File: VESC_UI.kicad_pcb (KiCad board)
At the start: 4 copper layers, 50 x 50 mm, 60 parts, among them J1 Hall_SS443A, J2 Hall_SS443A, J3 Conn_01x07_Male, J4 Conn_01x09_Female, J5 Conn_01x05_Male, J6 Conn_01x04_Male, J8 Conn_01x02_Male, J9 Conn_01x02_Male, Q1 Q_0010-DVB_Q, Q2 Q_0010-DVB_Q, SW1 SW_Push, SW2 SW_Push, SW3 SW_Push, SW4 SW_Push, SW5 SW_Push, U2 STM32F401CEUx, U3 M95M04-DR, Y1 Crystal_GND24_Small

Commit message: Modify some areas
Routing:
- added copper zone on B.Cu, net GND
- removed copper zone on B.Cu, net (none)

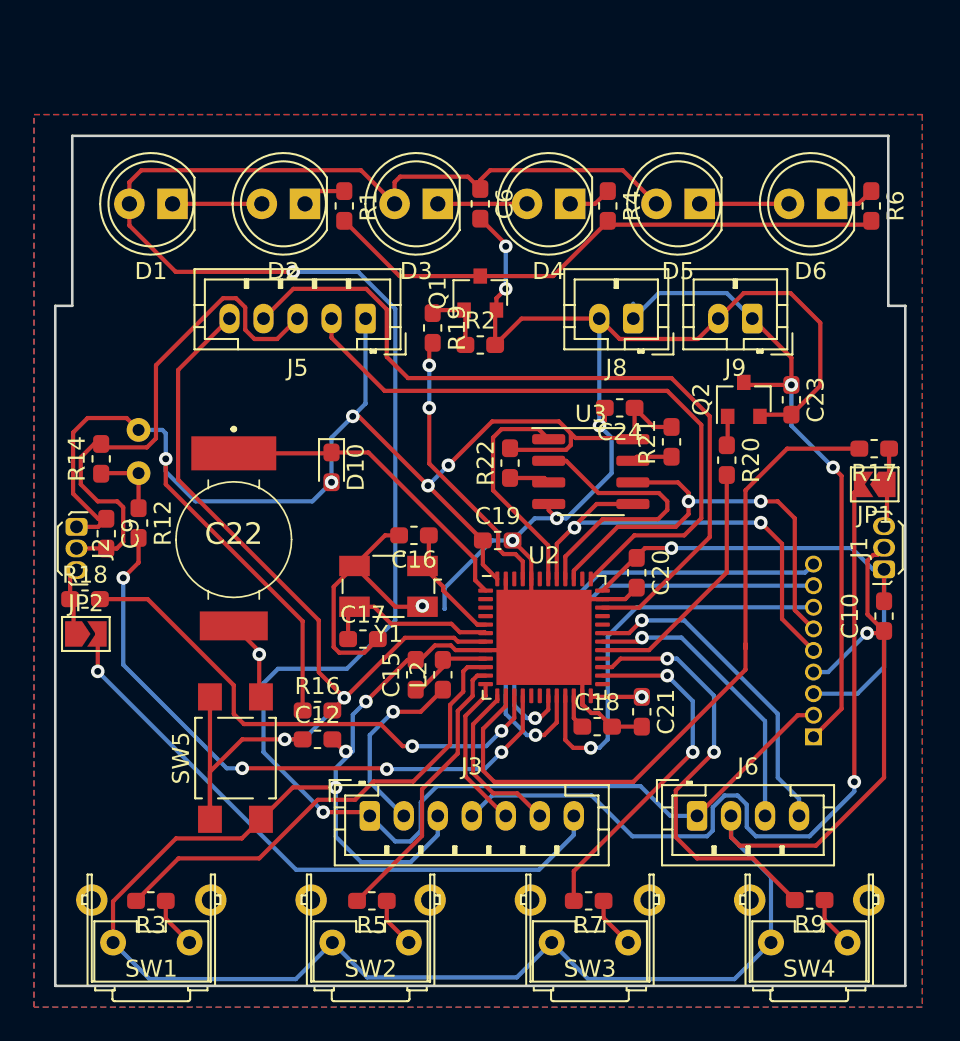
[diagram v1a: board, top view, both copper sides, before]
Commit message: fix: add missing rules and components
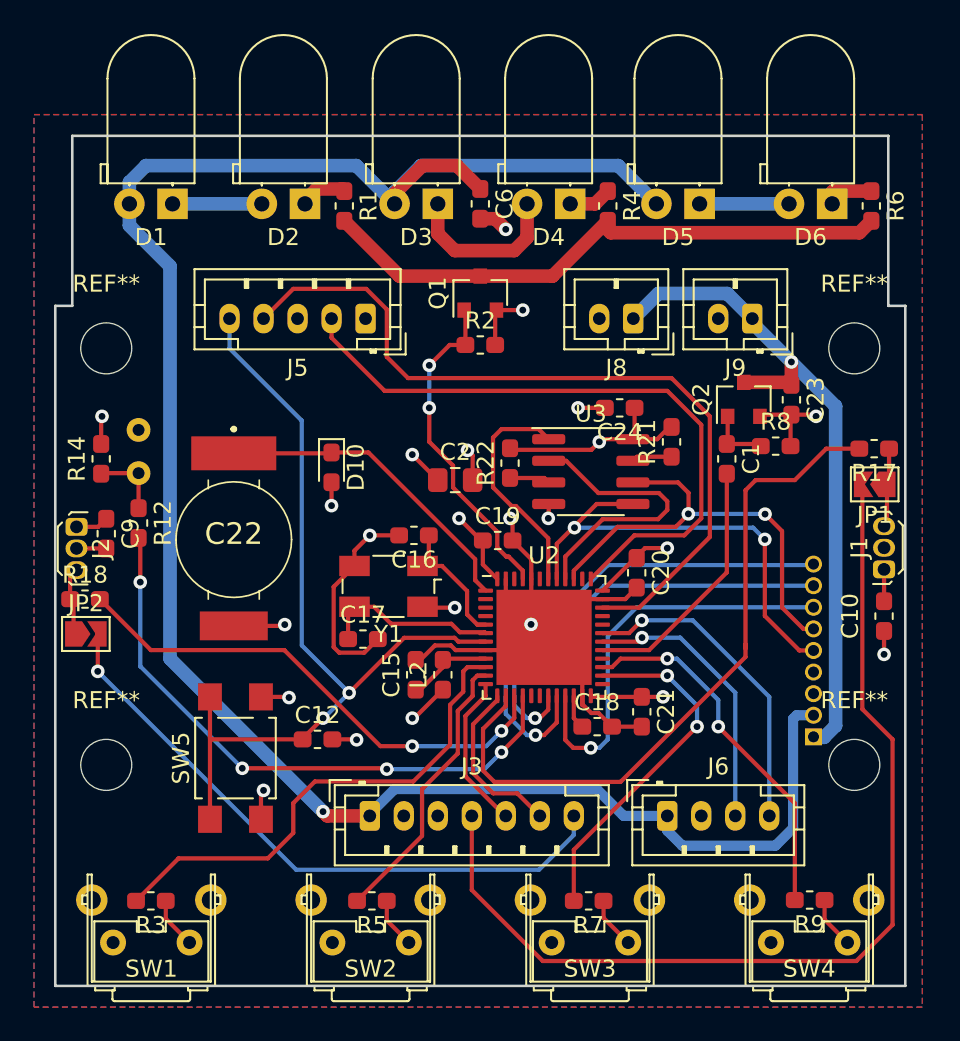
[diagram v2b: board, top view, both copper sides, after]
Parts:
- removed R16: R_Small, Resistor_SMD:R_0603_1608Metric_Pad1.05x0.95mm_HandSolder
- removed R19, R20: R_0020, Resistor_SMD:R_0603_1608Metric_Pad1.05x0.95mm_HandSolder
- added C1: C_Small, Capacitor_SMD:C_0603_1608Metric_Pad1.05x0.95mm_HandSolder, F.Cu at (153.5, 94.0)
- added C2: C_0003-DVB_C, Capacitor_SMD:C_0805_2012Metric_Pad1.15x1.40mm_HandSolder, F.Cu at (137.5, 95.2)
- added R8: R_Small, Resistor_SMD:R_0603_1608Metric_Pad1.05x0.95mm_HandSolder, F.Cu at (156.4, 93.2)
- added REF**: MountingHole_3.2mm_M3_DIN965, MountingHole:MountingHole_3.2mm_M3_DIN965, F.Cu at (161.0, 112.0)
- added REF**: MountingHole_3.2mm_M3_DIN965, MountingHole:MountingHole_3.2mm_M3_DIN965, F.Cu at (117.0, 112.0)
- added REF**: MountingHole_3.2mm_M3_DIN965, MountingHole:MountingHole_3.2mm_M3_DIN965, F.Cu at (117.0, 87.5)
- added REF**: MountingHole_3.2mm_M3_DIN965, MountingHole:MountingHole_3.2mm_M3_DIN965, F.Cu at (161.0, 87.5)
- D1, D2, D3, D4, D5, D6: footprint LED_THT:LED_D5.0mm_Clear -> LED_THT:LED_D5.0mm_Horizontal_O1.27mm_Z3.0mm_Clear
- moved J6 1.75 mm to (150.0, 115.0)
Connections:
- Q1 pad 1: Net-(Q1-Pad1) -> /LIGHT_SW
- R2 pad 1: Net-(Q1-Pad1) -> /LIGHT_SW
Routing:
- net GND: track 277.8 -> 80.4 mm, vias 11 -> 16
- net +3V3: track 137.2 -> 35.8 mm, vias 8 -> 7
- net /Accelerator: track 46.9 -> 58.4 mm, vias 1 -> 0
- net /NRST: track 59.3 -> 51.0 mm
- net +5V: track 127.3 -> 121.8 mm, vias 2 -> 1
- net Net-(D3-Pad1): track 5.25 -> 9.72 mm
- net Net-(Q1-Pad1): track 4.00 -> 0.00 mm
- net /BUTTON_4: track 25.5 -> 21.7 mm
- net /LIGHT_SW: track 16.6 -> 19.6 mm
- net Net-(C1-Pad1): track 1.72 -> 3.70 mm
- net /PHOTO_RESISTOR: track 36.9 -> 35.6 mm
- net /BUTTON_1: track 28.3 -> 29.4 mm
- net /ADC2: track 30.9 -> 30.0 mm
- net /SPI1_SCK: track 27.0 -> 26.2 mm
- net Net-(Q1-Pad3): track 33.9 -> 34.6 mm
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
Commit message: fix: change screen connector footprint and adjust its mechanical position
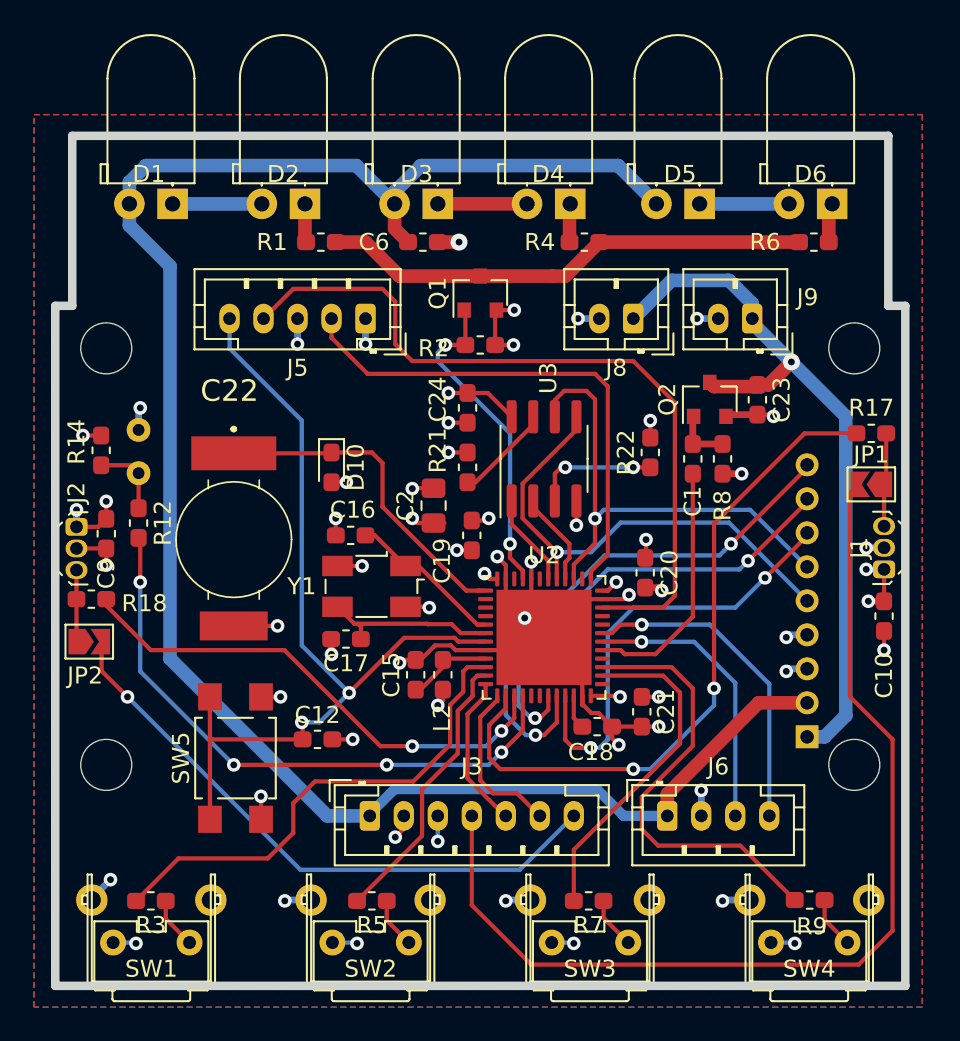
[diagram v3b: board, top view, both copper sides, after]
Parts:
- J4: footprint Connector_PinHeader_1.27mm:PinHeader_1x09_P1.27mm_Vertical -> Connector_PinHeader_2.00mm:PinHeader_1x09_P2.00mm_Vertical
- moved R21 12.1 mm to (138.2, 94.5)
- moved C24 8.95 mm to (138.2, 91.0), turned to 270 degrees
- moved R22 8.27 mm to (149.0, 93.6)
- moved C6 4.06 mm to (135.6, 81.2), turned to 0 degrees
- moved R6 3.99 mm to (158.6, 81.2), turned to 180 degrees
- moved C16 3.72 mm to (131.4, 98.5)
- moved R8 3.21 mm to (153.2, 94.0), turned to 270 degrees
- moved U3 2.85 mm to (142.8, 94.0), turned to 90 degrees
- moved R1 2.53 mm to (129.6, 81.2), turned to 0 degrees
- moved R4 2.53 mm to (145.1, 81.2), turned to 0 degrees
- moved C1 2.00 mm to (151.5, 94.0)
- moved C23 2.00 mm to (155.3, 90.5)
- moved Q2 2.00 mm to (152.5, 90.5)
- moved C2 1.97 mm to (136.2, 96.8), turned to 90 degrees
- moved C19 1.55 mm to (138.5, 98.5), turned to 90 degrees
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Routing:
- net GND: track 80.4 -> 93.4 mm, vias 16 -> 43
- net /SPI1_MISO: track 16.9 -> 5.57 mm
- net +5V: track 121.8 -> 112.4 mm, vias 1 -> 0
- net /SWDCLK: track 38.5 -> 30.3 mm
- net /EXT_FLASH_CS: track 13.5 -> 6.28 mm
- net Net-(Q1-Pad3): track 34.6 -> 28.9 mm
- net +3V3: track 35.8 -> 30.4 mm, vias 7 -> 20
- net Net-(R22-Pad1): track 2.38 -> 7.38 mm, vias 0 -> 2
- net Net-(D3-Pad1): track 9.72 -> 5.25 mm
- net /BUTTON_4: track 21.7 -> 26.1 mm, vias 2 -> 0
- net Net-(R21-Pad1): track 2.37 -> 5.73 mm
- net +12V: track 40.0 -> 43.3 mm
- net /OLED_RST: track 28.8 -> 31.6 mm, vias 1 -> 2
- net /SPI1_SCK: track 26.2 -> 29.0 mm, vias 2 -> 1
- net /OLED_DC: track 24.9 -> 27.0 mm, vias 1 -> 2
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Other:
- net class power: trace_width 0.6 -> 0.8; via_dia 0.8 -> 1

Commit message: adjust vias drill dimension to comply PCB provider rules
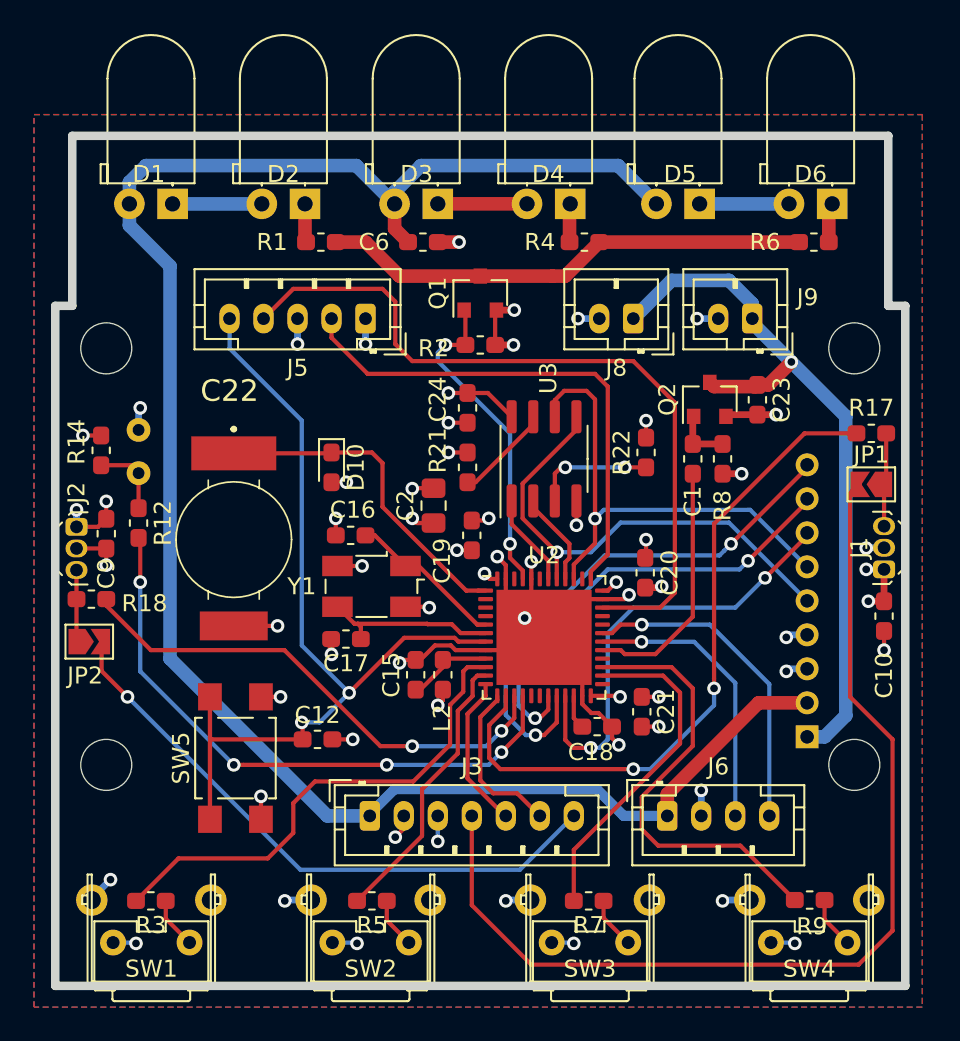
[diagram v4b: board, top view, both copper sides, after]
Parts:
- moved R22 0.25 mm to (148.8, 93.6)
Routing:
- net GND: track 93.4 -> 90.9 mm
- net Net-(J1-Pad3): track 6.02 -> 5.28 mm
- net +3V3: track 30.4 -> 29.8 mm
- net Net-(C17-Pad1): track 10.9 -> 10.3 mm
- net Net-(C16-Pad1): track 9.77 -> 9.24 mm
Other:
- net class Default: via_drill 0.4 -> 0.45
- net class power: via_drill 0.4 -> 0.45

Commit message: fix and refactor: both mainboard and screenboard
Many improvements made
- Fixed all issues with footprints
- Optimized components placement and tracks
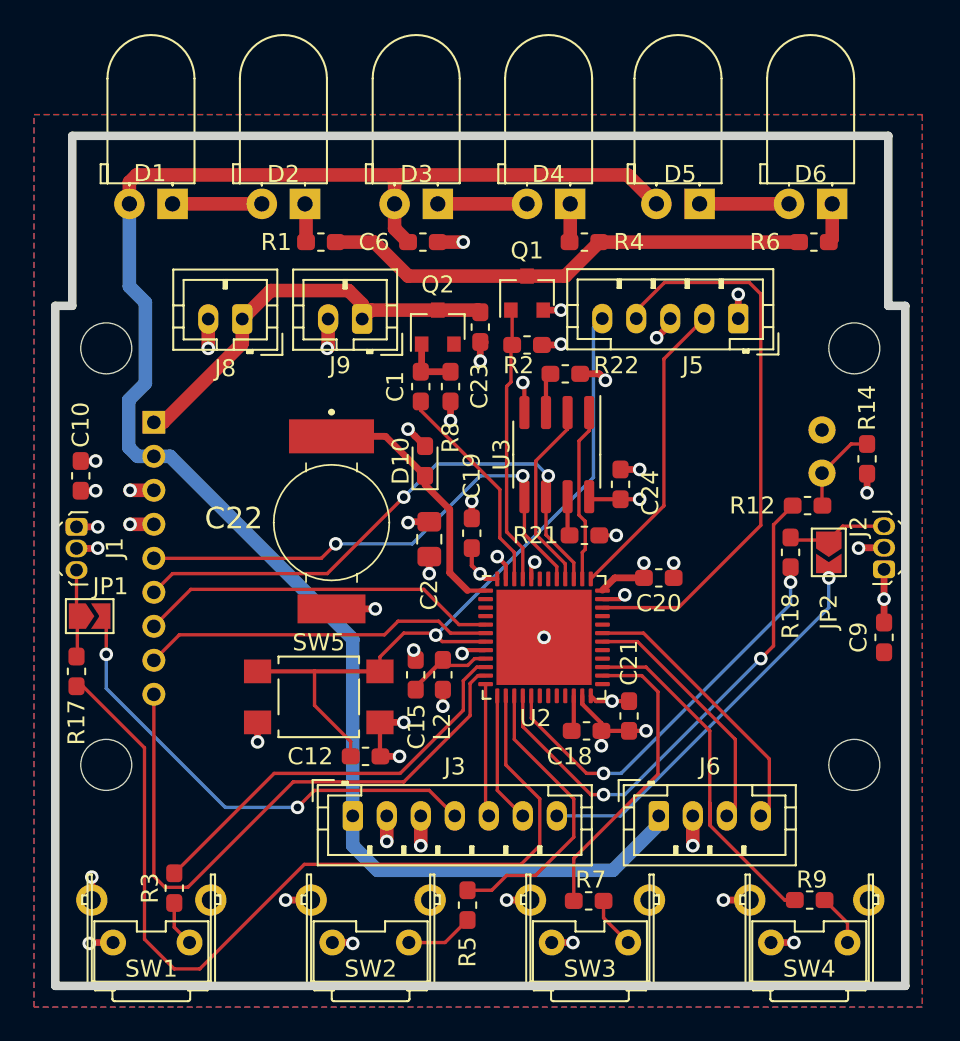
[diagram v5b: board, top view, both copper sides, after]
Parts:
- removed C16, C17: C_Small, Capacitor_SMD:C_0603_1608Metric_Pad1.05x0.95mm_HandSolder
- removed Y1: Crystal_GND24_Small, Crystal:Crystal_SMD_Abracon_ABM3B-4Pin_5.0x3.2mm
- R13: footprint Resistor_THT:R_Axial_DIN0204_L3.6mm_D1.6mm_P2.54mm_Vertical -> OptoDevice:R_LDR_4.9x4.2mm_P2.54mm_Vertical
- moved R17 48.8 mm to (115.2, 106.5), turned to 270 degrees
- moved C10 48.0 mm to (115.5, 95.0), turned to 90 degrees
- moved J1 47.6 mm to (115.2, 98.0), turned to 270 degrees
- moved J2 47.6 mm to (162.8, 100.5), turned to 90 degrees
- moved JP1 46.6 mm to (116.0, 103.2), turned to 0 degrees
- moved C9 46.2 mm to (162.8, 104.5)
- moved R14 45.1 mm to (161.8, 94.0), turned to 270 degrees
- moved JP2 43.8 mm to (159.5, 99.5), turned to 270 degrees
- moved J4 42.6 mm to (119.8, 91.8), turned to 180 degrees
- moved R18 41.2 mm to (157.2, 99.5), turned to 270 degrees
- moved R13 40.2 mm to (159.1, 92.3)
- moved R12 39.4 mm to (158.2, 96.8), turned to 180 degrees
- moved J8 23.0 mm to (125.0, 85.8)
- moved J9 23.0 mm to (132.1, 85.8)
- moved J5 21.9 mm to (154.2, 85.8)
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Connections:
- U2 pad 11: /BUTTON_2 -> /OLED_RST
- U2 pad 15: /ADC2 -> /BUTTON_2
- U2 pad 17: Net-(U2-Pad17) -> /ADC2
- U2 pad 19: /OLED_DC -> Net-(U2-Pad19)
- U2 pad 20: /OLED_RST -> Net-(U2-Pad20)
- U2 pad 21: /OLED_CS -> Net-(U2-Pad21)
- U2 pad 29: /BUZZER -> Net-(U2-Pad29)
- U2 pad 38: Net-(U2-Pad38) -> /EXT_FLASH_CS
- U2 pad 42: /EXT_FLASH_CS -> Net-(U2-Pad42)
- U2 pad 46: Net-(U2-Pad46) -> /BUZZER
- U2 pad 5: Net-(C16-Pad1) -> /OLED_CS
- U2 pad 6: Net-(C17-Pad1) -> /OLED_DC
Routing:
- net GND: track 90.9 -> 58.1 mm, vias 43 -> 40
- net /Accelerator: track 59.8 -> 28.8 mm, vias 0 -> 2
- net +12V: track 43.3 -> 24.7 mm, vias 1 -> 0
- net /ADC1: track 40.4 -> 53.4 mm, vias 2 -> 0
- net /SWDCLK: track 30.3 -> 18.1 mm
- net /Brake: track 35.7 -> 23.6 mm
- net /SWDIO: track 45.0 -> 33.7 mm
- net Net-(C17-Pad1): track 10.3 -> 0.00 mm
- net +5V: track 112.4 -> 102.9 mm
- net Net-(C16-Pad1): track 9.24 -> 0.00 mm
- net /NRST: track 51.6 -> 43.6 mm, vias 2 -> 1
- net /OLED_DC: track 27.0 -> 20.8 mm, vias 2 -> 0
- net /SPI1_MISO: track 5.57 -> 11.3 mm
- net /ADC2: track 29.8 -> 24.2 mm
- net /OLED_RST: track 31.6 -> 36.7 mm, vias 2 -> 0
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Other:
- net class Default: trace_width 0.25 -> 0.2
- net class bigPower added: clearance 0.4, trace_width 0.8, via_dia 1, via_drill 0.45
- net class power: clearance 0.4 -> 0.2; trace_width 0.8 -> 0.4; via_dia 1 -> 0.8

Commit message: Finalize new board
- Remove some useless components
- Change some footprints according to components availability
- Optimize tracks and placements
- Fix bad LDR and screen location
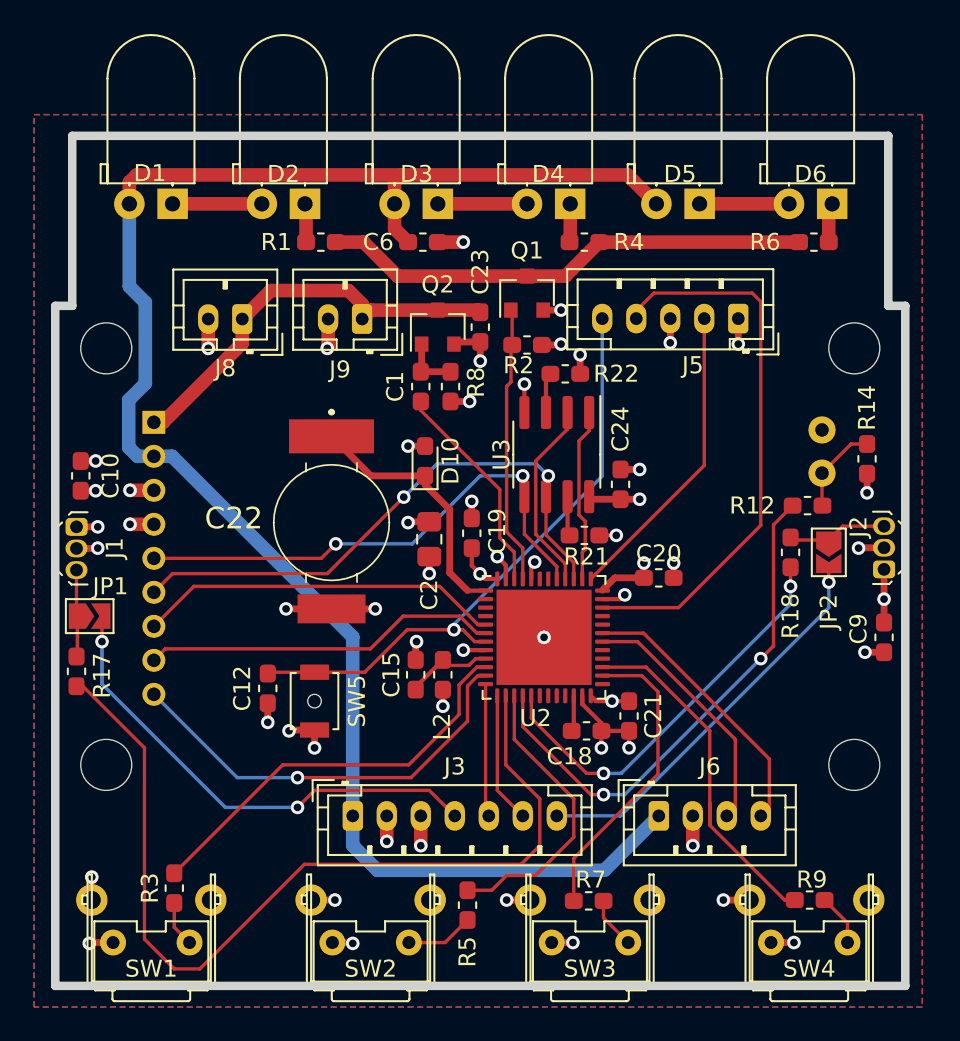
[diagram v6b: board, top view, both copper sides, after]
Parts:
- C1: value C_Small -> 10n
- C10, C19, C20, C21, C6, C9: value C_Small -> 100n
- C12, C15, C23, C24: value C_0033 -> 100n
- C2: value C_0003-DVB_C -> 10µF
- C22: value CP_Small -> SUpercap 330mF
- D1, D2, D3, D4, D5, D6: value LED_Small_ALT -> LED 5mm - White
- D10: value D_Schottky_Small_ALT -> Schottky CD0603-B0240R
- J1, J2: value Hall_SS443A -> Hall_SS441R
- L2: value MMZ1608B121C -> MMZ1608B121CTDH5
- Q1, Q2: value Q_0010-DVB_Q -> Mosfet IRLML2060TRPBF
- R1, R4, R6: value R_0020 -> 30
- R12, R3, R5, R7, R9: value R_Small -> 100
- R13: value R_PHOTO -> NSL-19M51
- R14: value R_0020 -> 10k
- R17, R18: value R_Small -> 0
- R2: value R_0020 -> 100k
- R21, R22: value R_Small -> 10k
- R8: value R_Small -> 1M
- SW1, SW2, SW3, SW4: value SW_Push -> Vertical push button
- SW5: value SW_Push -> Push button; footprint Button_Switch_SMD:SW_SPST_TL3305A -> Button_Switch_SMD:SW_SPST_B3U-1000P-B
- U2: value STM32F401CEUx -> STM32F401CEU6
- moved C12 7.00 mm to (126.5, 107.5), turned to 270 degrees
- moved SW5 0.35 mm to (129.2, 108.2), turned to 270 degrees
- turned C6 to 180 degrees
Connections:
- C6 pad 1: +5V -> GND
- C6 pad 2: GND -> +5V
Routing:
- net /OLED_RST: track 36.7 -> 25.2 mm, vias 0 -> 1
- net /NRST: track 43.6 -> 36.8 mm
- net GND: track 58.1 -> 61.6 mm, vias 40 -> 42
- net +3V3: track 27.0 -> 26.1 mm
- net /SWDIO: track 33.7 -> 32.9 mm
